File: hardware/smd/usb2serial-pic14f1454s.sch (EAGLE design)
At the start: 14 parts, among them IC1 PIC16F1454, IC2 TLV760-33, J1 USB-SHIELD-A-H, J2 J2

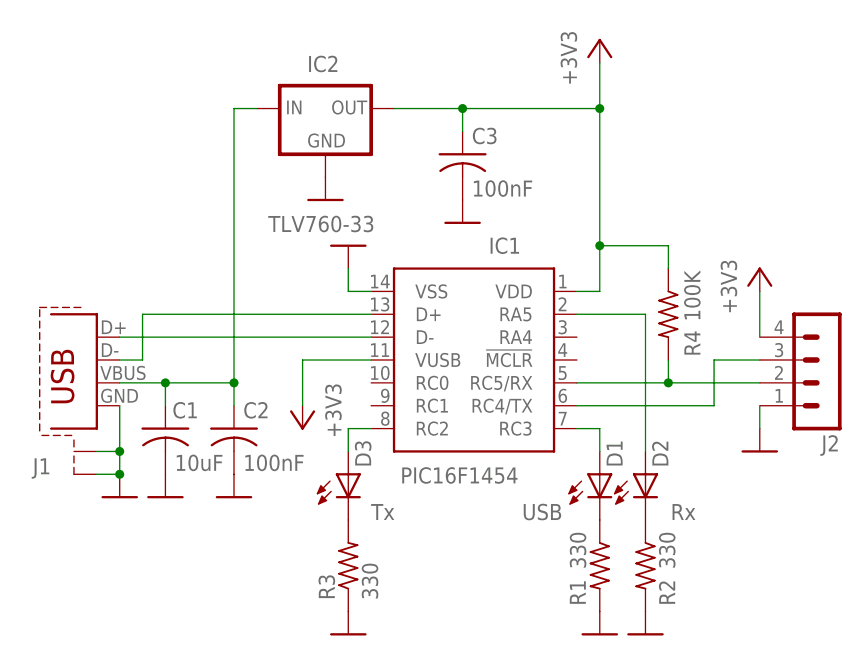
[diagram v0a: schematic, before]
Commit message: Fixed D+/D- bug
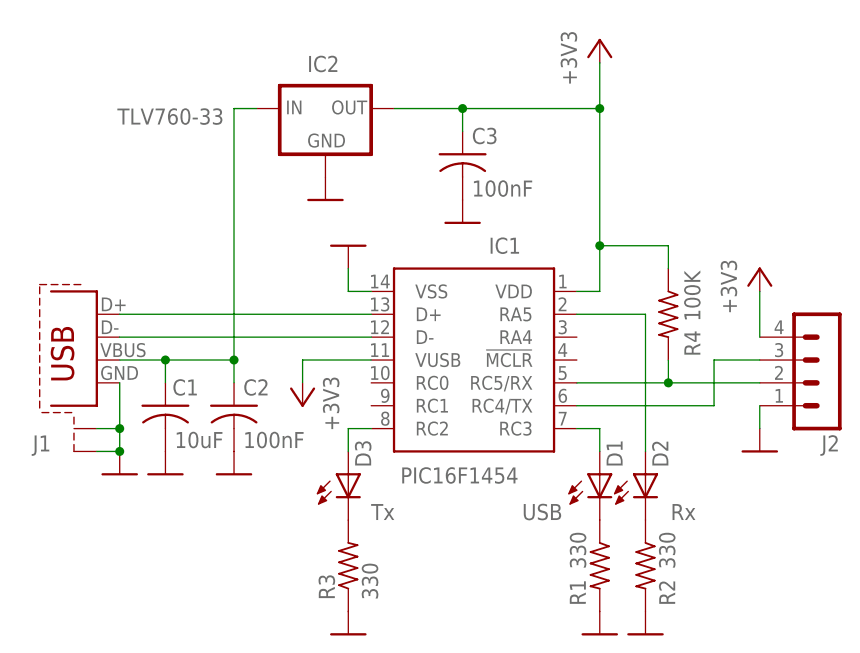
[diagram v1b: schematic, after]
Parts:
- IC1: device obddiag-net:PIC16F1454SOIC -> obddiag-net:PIC16F1454-SOIC
- J1: value USB-SHIELD-A-H -> USB-SHIELD-A-H1; device obddiag-net:USB-SHIELD-A-H -> obddiag-net:USB-SHIELD-A-H1
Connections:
- net N$3: now also IC1.D-; no longer IC1.D+
- net N$4: now also IC1.D+; no longer IC1.D-
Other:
- moved on the sheet: C1, C2, J1
